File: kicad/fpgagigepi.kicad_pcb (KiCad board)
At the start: 2 copper layers, 1 part, among them U1 24LC32

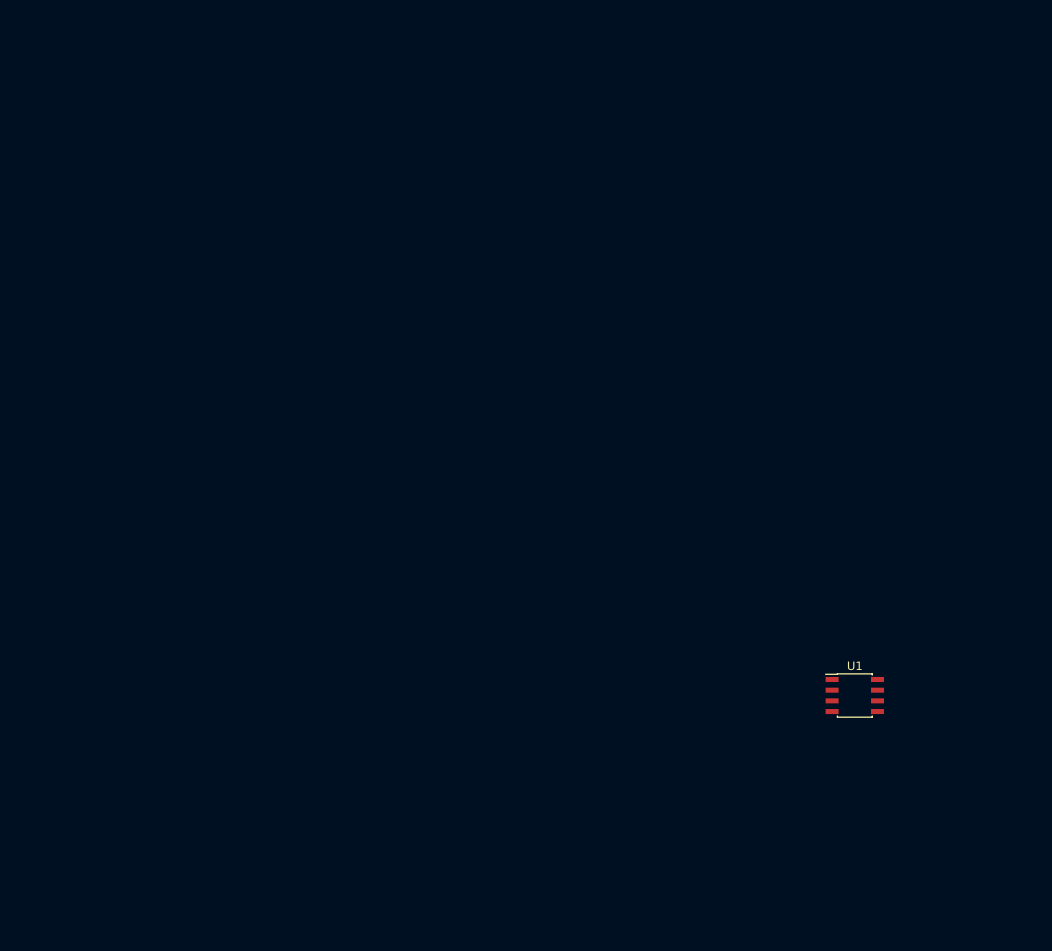
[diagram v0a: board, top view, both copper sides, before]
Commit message: place components to pcb, add footprints of cfps-73 l829 sot-563
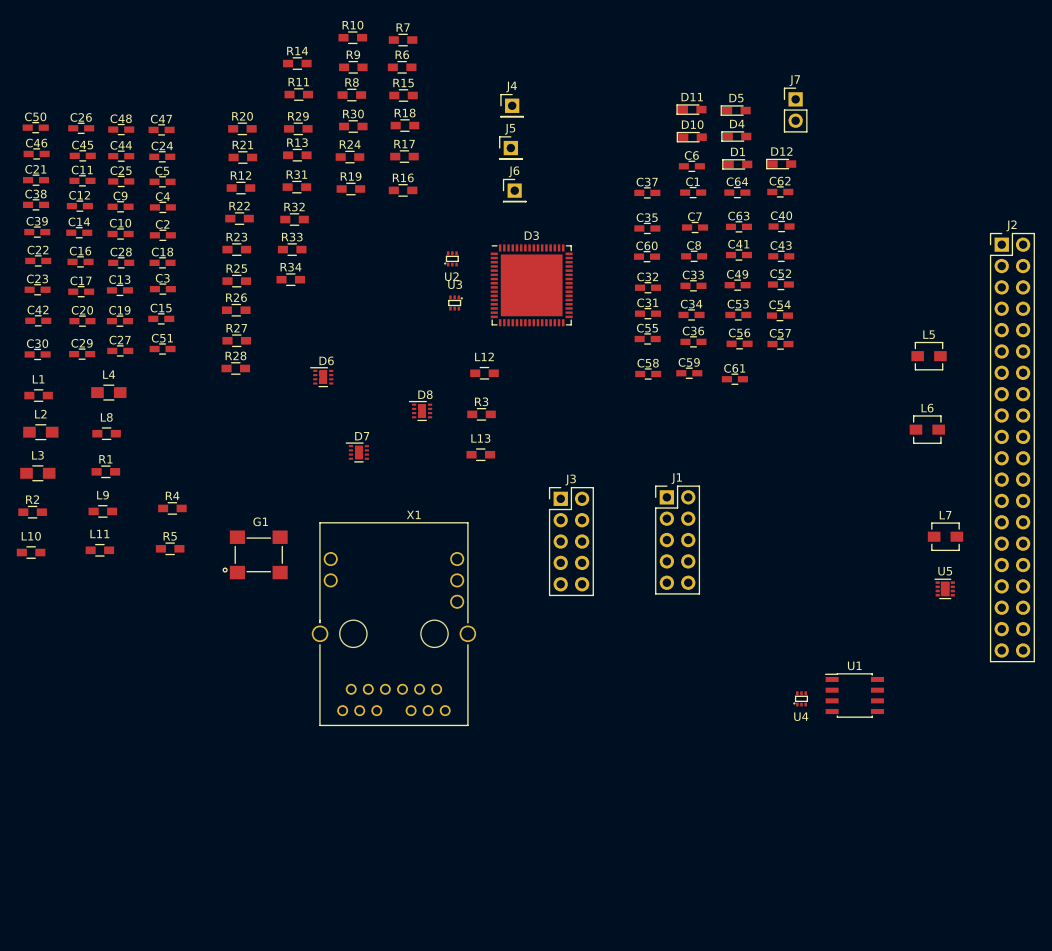
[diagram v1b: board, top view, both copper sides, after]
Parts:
- added C1: 0.1u 16V, Capacitors_SMD:C_0603_HandSoldering, F.Cu at (129.3, 45.2)
- added C10: 22u 6v3, Capacitors_SMD:C_0603_HandSoldering, F.Cu at (61.2, 50.1)
- added C11: 22u 6v3, Capacitors_SMD:C_0603_HandSoldering, F.Cu at (56.6, 43.8)
- added C12: 22u 6v3, Capacitors_SMD:C_0603_HandSoldering, F.Cu at (56.3, 46.8)
- added C13: 10u, Capacitors_SMD:C_0603_HandSoldering, F.Cu at (61.1, 56.8)
- added C14: 10u, Capacitors_SMD:C_0603_HandSoldering, F.Cu at (56.3, 50.0)
- added C15: 0.1u, Capacitors_SMD:C_0603_HandSoldering, F.Cu at (66.0, 60.2)
- added C16: 0.1u, Capacitors_SMD:C_0603_HandSoldering, F.Cu at (56.4, 53.4)
- added C17: 10u, Capacitors_SMD:C_0603_HandSoldering, F.Cu at (56.5, 57.0)
- added C18: 0.1u, Capacitors_SMD:C_0603_HandSoldering, F.Cu at (66.2, 53.5)
- added C19: 0.1u, Capacitors_SMD:C_0603_HandSoldering, F.Cu at (61.1, 60.5)
- added C2: 0.1u 16V, Capacitors_SMD:C_0603_HandSoldering, F.Cu at (66.2, 50.3)
- added C20: 10u, Capacitors_SMD:C_0603_HandSoldering, F.Cu at (56.6, 60.5)
- added C21: 0.1u, Capacitors_SMD:C_0603_HandSoldering, F.Cu at (51.1, 43.7)
- added C22: 0.1u, Capacitors_SMD:C_0603_HandSoldering, F.Cu at (51.4, 53.3)
- added C23: 0.1u, Capacitors_SMD:C_0603_HandSoldering, F.Cu at (51.3, 56.7)
- added C24: 0.1u, Capacitors_SMD:C_0603_HandSoldering, F.Cu at (66.1, 40.9)
- added C25: 0.1u, Capacitors_SMD:C_0603_HandSoldering, F.Cu at (61.3, 43.9)
- added C26: 0.1u, Capacitors_SMD:C_0603_HandSoldering, F.Cu at (56.5, 37.5)
- added C27: 0.1u, Capacitors_SMD:C_0603_HandSoldering, F.Cu at (61.1, 64.0)
- added C28: 0.1u, Capacitors_SMD:C_0603_HandSoldering, F.Cu at (61.3, 53.5)
- added C29: 0.01u, Capacitors_SMD:C_0603_HandSoldering, F.Cu at (56.6, 64.4)
- added C3: 0.1u 16V, Capacitors_SMD:C_0603_HandSoldering, F.Cu at (66.2, 56.7)
- added C30: 0.01u, Capacitors_SMD:C_0603_HandSoldering, F.Cu at (51.3, 64.4)
- added C31: 0.01u, Capacitors_SMD:C_0603_HandSoldering, F.Cu at (123.9, 59.6)
- added C32: 0.01u, Capacitors_SMD:C_0603_HandSoldering, F.Cu at (123.9, 56.5)
- added C33: 0.01u, Capacitors_SMD:C_0603_HandSoldering, F.Cu at (129.3, 56.3)
- added C34: 0.1u, Capacitors_SMD:C_0603_HandSoldering, F.Cu at (129.1, 59.7)
- added C35: 0.01u, Capacitors_SMD:C_0603_HandSoldering, F.Cu at (123.8, 49.5)
- added C36: 0.1u, Capacitors_SMD:C_0603_HandSoldering, F.Cu at (129.3, 62.9)
- added C37: 0.01u, Capacitors_SMD:C_0603_HandSoldering, F.Cu at (123.8, 45.2)
- added C38: 0.1u, Capacitors_SMD:C_0603_HandSoldering, F.Cu at (51.1, 46.6)
- added C39: 0.01u, Capacitors_SMD:C_0603_HandSoldering, F.Cu at (51.3, 49.9)
- added C4: 0.1u 16V, Capacitors_SMD:C_0603_HandSoldering, F.Cu at (66.2, 47.0)
- added C40: 0.1u, Capacitors_SMD:C_0603_HandSoldering, F.Cu at (139.8, 49.2)
- added C41: 0.1u, Capacitors_SMD:C_0603_HandSoldering, F.Cu at (134.7, 52.6)
- added C42: 10u, Capacitors_SMD:C_0603_HandSoldering, F.Cu at (51.4, 60.4)
- added C43: 0.1u, Capacitors_SMD:C_0603_HandSoldering, F.Cu at (139.8, 52.8)
- added C44: 10u, Capacitors_SMD:C_0603_HandSoldering, F.Cu at (61.3, 40.9)
- added C45: 0.1u, Capacitors_SMD:C_0603_HandSoldering, F.Cu at (56.7, 40.8)
- added C46: 0.1u, Capacitors_SMD:C_0603_HandSoldering, F.Cu at (51.2, 40.6)
- added C47: 0.1u, Capacitors_SMD:C_0603_HandSoldering, F.Cu at (66.1, 37.7)
- added C48: 10u, Capacitors_SMD:C_0603_HandSoldering, F.Cu at (61.3, 37.7)
- added C49: 0.1u, Capacitors_SMD:C_0603_HandSoldering, F.Cu at (134.6, 56.2)
- added C5: 0.1u, Capacitors_SMD:C_0603_HandSoldering, F.Cu at (66.2, 43.9)
- added C50: 0.1u, Capacitors_SMD:C_0603_HandSoldering, F.Cu at (51.1, 37.5)
- added C51: 0.1u, Capacitors_SMD:C_0603_HandSoldering, F.Cu at (66.2, 63.8)
- added C52: 0.1u, Capacitors_SMD:C_0603_HandSoldering, F.Cu at (139.7, 56.1)
- added C53: 0.1u, Capacitors_SMD:C_0603_HandSoldering, F.Cu at (134.6, 59.7)
- added C54: 0.1u, Capacitors_SMD:C_0603_HandSoldering, F.Cu at (139.6, 59.8)
- added C55: 0.1u, Capacitors_SMD:C_0603_HandSoldering, F.Cu at (123.9, 62.6)
- added C56: 0.1u, Capacitors_SMD:C_0603_HandSoldering, F.Cu at (134.8, 63.2)
- added C57: 0.1u, Capacitors_SMD:C_0603_HandSoldering, F.Cu at (139.7, 63.2)
- added C58: 0.1u, Capacitors_SMD:C_0603_HandSoldering, F.Cu at (123.9, 66.8)
- added C59: 0.1u, Capacitors_SMD:C_0603_HandSoldering, F.Cu at (128.8, 66.7)
- added C6: 0.1u, Capacitors_SMD:C_0603_HandSoldering, F.Cu at (129.1, 42.1)
- added C60: 10u, Capacitors_SMD:C_0603_HandSoldering, F.Cu at (123.8, 52.8)
- added C61: 10u, Capacitors_SMD:C_0603_HandSoldering, F.Cu at (134.2, 67.4)
- added C62: 10u, Capacitors_SMD:C_0603_HandSoldering, F.Cu at (139.6, 45.1)
- added C63: 0.1u, Capacitors_SMD:C_0603_HandSoldering, F.Cu at (134.7, 49.3)
- added C64: 10u, Capacitors_SMD:C_0603_HandSoldering, F.Cu at (134.5, 45.2)
- added C7: 10u 16V, Capacitors_SMD:C_0603_HandSoldering, F.Cu at (129.5, 49.3)
- added C8: 10u 16V, Capacitors_SMD:C_0603_HandSoldering, F.Cu at (129.4, 52.8)
- added C9: 10u 16V, Capacitors_SMD:C_0603_HandSoldering, F.Cu at (61.2, 46.9)
- added D1: LED, LEDs:LED_0603_HandSoldering, F.Cu at (134.6, 41.8)
- added D10: LED, LEDs:LED_0603_HandSoldering, F.Cu at (129.2, 38.6)
- added D11: LED, LEDs:LED_0603_HandSoldering, F.Cu at (129.2, 35.3)
- added D12: LED, LEDs:LED_0603_HandSoldering, F.Cu at (139.8, 41.8)
- added D3: KSZ9021GN, Housings_DFN_QFN:QFN-64-1EP_9x9mm_Pitch0.5mm, F.Cu at (110.1, 56.2)
- added D4: LED, LEDs:LED_0603_HandSoldering, F.Cu at (134.5, 38.5)
- added D5: LED, LEDs:LED_0603_HandSoldering, F.Cu at (134.4, 35.4)
- added D6: TLV62084, Housings_SON:WSON-8_1EP_2x2mm_Pitch0.5mm, F.Cu at (85.3, 67.1)
- added D7: TLV62084, Housings_SON:WSON-8_1EP_2x2mm_Pitch0.5mm, F.Cu at (89.5, 76.1)
- added D8: TLV62080, Housings_SON:WSON-8_1EP_2x2mm_Pitch0.5mm, F.Cu at (97.0, 71.2)
- added G1: CFPS-73, library:CFPS-73, F.Cu at (77.6, 88.3)
- added J1: Conn_02x05_Odd_Even, Pin_Headers:Pin_Header_Straight_2x05_Pitch2.54mm, F.Cu at (126.1, 81.4)
- added J2: Conn_02x20_Odd_Even, Pin_Headers:Pin_Header_Straight_2x20_Pitch2.54mm, F.Cu at (166.0, 51.4)
- added J3: Conn_02x05_Odd_Even, Pin_Headers:Pin_Header_Straight_2x05_Pitch2.54mm, F.Cu at (113.5, 81.6)
- added J4: Conn_01x01, Pin_Headers:Pin_Header_Straight_1x01_Pitch2.54mm, F.Cu at (107.7, 34.9)
- added J5: Conn_01x01, Pin_Headers:Pin_Header_Straight_1x01_Pitch2.54mm, F.Cu at (107.6, 39.9)
- added J6: Conn_01x01, Pin_Headers:Pin_Header_Straight_1x01_Pitch2.54mm, F.Cu at (108.1, 45.0)
- added J7: Conn_01x02, Pin_Headers:Pin_Header_Straight_1x02_Pitch2.54mm, F.Cu at (141.5, 34.1)
- added L1: BLM18PG330, Inductors_SMD:L_0603_HandSoldering, F.Cu at (51.4, 69.3)
- added L10: BLM18PG330, Inductors_SMD:L_0603_HandSoldering, F.Cu at (50.5, 88.0)
- added L11: BLM18PG330, Inductors_SMD:L_0603_HandSoldering, F.Cu at (58.7, 87.7)
- added L12: BLM18PG330, Inductors_SMD:L_0603_HandSoldering, F.Cu at (104.5, 66.7)
- added L13: BLM18PG330, Inductors_SMD:L_0603_HandSoldering, F.Cu at (104.0, 76.4)
- added L2: BLM21PG300, Inductors_SMD:L_0805_HandSoldering, F.Cu at (51.7, 73.7)
- added L3: BLM21PG300, Inductors_SMD:L_0805_HandSoldering, F.Cu at (51.3, 78.6)
- added L4: BLM21PG300, Inductors_SMD:L_0805_HandSoldering, F.Cu at (59.8, 69.0)
- added L5: LQH3NPN1R0NJ0L, Inductors_SMD:L_Vishay_IHLP-1212, F.Cu at (157.3, 64.6)
- added L6: LQH3NPN1R0NJ0L, Inductors_SMD:L_Vishay_IHLP-1212, F.Cu at (157.1, 73.4)
- added L7: LQH3NPN1R0NJ0L, Inductors_SMD:L_Vishay_IHLP-1212, F.Cu at (159.3, 86.1)
- added L8: BLM18PG330, Inductors_SMD:L_0603_HandSoldering, F.Cu at (59.5, 73.9)
- added L9: BLM18PG330, Inductors_SMD:L_0603_HandSoldering, F.Cu at (59.1, 83.1)
- added R1: 3.9k, Resistors_SMD:R_0603_HandSoldering, F.Cu at (59.4, 78.4)
- added R10: 39.2k 1%, Resistors_SMD:R_0603_HandSoldering, F.Cu at (88.8, 26.8)
- added R11: 178k 1%, Resistors_SMD:R_0603_HandSoldering, F.Cu at (82.4, 33.5)
- added R12: 39.2k 1%, Resistors_SMD:R_0603_HandSoldering, F.Cu at (75.5, 44.6)
- added R13: 10k, Resistors_SMD:R_0603_HandSoldering, F.Cu at (82.2, 40.7)
- added R14: 4.7k, Resistors_SMD:R_0603_HandSoldering, F.Cu at (82.2, 29.8)
- added R15: 390, Resistors_SMD:R_0603_HandSoldering, F.Cu at (94.8, 33.6)
- added R16: 390, Resistors_SMD:R_0603_HandSoldering, F.Cu at (94.8, 44.9)
- added R17: 390, Resistors_SMD:R_0603_HandSoldering, F.Cu at (94.9, 40.9)
- added R18: 390, Resistors_SMD:R_0603_HandSoldering, F.Cu at (95.0, 37.2)
- added R19: 10k, Resistors_SMD:R_0603_HandSoldering, F.Cu at (88.6, 44.8)
- added R2: 3.9k, Resistors_SMD:R_0603_HandSoldering, F.Cu at (50.7, 83.2)
- added R20: 10k, Resistors_SMD:R_0603_HandSoldering, F.Cu at (75.7, 37.6)
- added R21: 4.7k, Resistors_SMD:R_0603_HandSoldering, F.Cu at (75.7, 41.0)
- added R22: 220, Resistors_SMD:R_0603_HandSoldering, F.Cu at (75.3, 48.3)
- added R23: 220, Resistors_SMD:R_0603_HandSoldering, F.Cu at (75.0, 52.0)
- added R24: 10k, Resistors_SMD:R_0603_HandSoldering, F.Cu at (88.5, 41.0)
- added R25: 1k, Resistors_SMD:R_0603_HandSoldering, F.Cu at (75.0, 55.7)
- added R26: 1k, Resistors_SMD:R_0603_HandSoldering, F.Cu at (74.9, 59.2)
- added R27: 1k, Resistors_SMD:R_0603_HandSoldering, F.Cu at (75.0, 62.8)
- added R28: 10k, Resistors_SMD:R_0603_HandSoldering, F.Cu at (74.9, 66.1)
- added R29: 10k, Resistors_SMD:R_0603_HandSoldering, F.Cu at (82.3, 37.6)
- added R3: 1k, Resistors_SMD:R_0603_HandSoldering, F.Cu at (104.1, 71.6)
- added R30: 10k, Resistors_SMD:R_0603_HandSoldering, F.Cu at (88.8, 37.3)
- added R31: 10k, Resistors_SMD:R_0603_HandSoldering, F.Cu at (82.1, 44.5)
- added R32: 390, Resistors_SMD:R_0603_HandSoldering, F.Cu at (81.9, 48.4)
- added R33: 390, Resistors_SMD:R_0603_HandSoldering, F.Cu at (81.6, 52.0)
- added R34: 4.99k 1%, Resistors_SMD:R_0603_HandSoldering, F.Cu at (81.4, 55.5)
- added R4: 10k, Resistors_SMD:R_0603_HandSoldering, F.Cu at (67.3, 82.8)
- added R5: 10k, Resistors_SMD:R_0603_HandSoldering, F.Cu at (67.1, 87.6)
- added R6: 1k, Resistors_SMD:R_0603_HandSoldering, F.Cu at (94.7, 30.3)
- added R7: 178k 1%, Resistors_SMD:R_0603_HandSoldering, F.Cu at (94.8, 27.0)
- added R8: 28k 1%, Resistors_SMD:R_0603_HandSoldering, F.Cu at (88.7, 33.6)
- added R9: 65.3k 1%, Resistors_SMD:R_0603_HandSoldering, F.Cu at (88.8, 30.3)
- added U2: NUP4114UPXV6T1G, library:SOT-563-6, F.Cu at (100.6, 53.1)
- added U3: NUP4114UPXV6T1G, library:SOT-563-6, F.Cu at (100.9, 58.3)
- added U4: NUP4114UPXV6T1G, library:SOT-563-6, F.Cu at (142.2, 105.4)
- added U5: NB3L553, Housings_DFN_QFN:DFN-8-1EP_2x2mm_Pitch0.5mm, F.Cu at (159.3, 92.3)
- added X1: L829-1J1T-43, library:L829, F.Cu at (93.7, 97.7)

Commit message: add modeles to 3d render
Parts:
- added D2: 10cl025, library:EQFP-144_20x20mm_Pitch0.5mm, F.Cu at (120.3, 92.3)
- C11, C12, C14, C21, C24, C25, C26, C38, C39, C44, C45, C46, C47, C48, C5, C50, C52, C54, C62, C9, L11, L12, L8, L9, R1, R3: moved to B.Cu
- D6, D7, D8: footprint Housings_SON:WSON-8_1EP_2x2mm_Pitch0.5mm -> library:WSON-8_1EP_2x2mm_Pitch0.5mm
- J2: footprint Pin_Headers:Pin_Header_Straight_2x20_Pitch2.54mm -> Socket_Strips:Socket_Strip_Straight_2x20_Pitch2.54mm; moved to B.Cu
- L5, L6, L7: footprint Inductors_SMD:L_Vishay_IHLP-1212 -> library:L_Vishay_IHLP-1212
- moved R2 106.0 mm to (156.3, 92.2)
- moved R7 105.9 mm to (143.8, 120.9)
- moved R6 104.6 mm to (143.8, 122.6)
- moved R14 104.1 mm to (131.2, 121.7)
- moved R9 103.8 mm to (139.5, 120.9)
- moved R8 102.5 mm to (139.5, 122.6)
- moved R33 102.3 mm to (156.0, 122.1)
- moved R10 101.1 mm to (123.3, 121.8), turned to 180 degrees
- moved C29 97.6 mm to (135.9, 121.3), turned to 90 degrees
- moved C50 97.4 mm to (108.7, 116.0)
- moved C26 97.2 mm to (114.1, 115.9)
- moved C48 97.0 mm to (118.9, 115.7)
- moved C47 96.9 mm to (123.7, 115.7)
- moved L2 93.9 mm to (143.4, 93.8)
- moved C46 92.4 mm to (108.8, 112.8)
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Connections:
- J4 pad 1: +3V3 -> Net-(C10-Pad1)
- J5 pad 1: +1V2 -> Net-(C11-Pad1)
- J6 pad 1: +2V5 -> Net-(C12-Pad1)
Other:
- board outline added: 65 x 56.5 mm

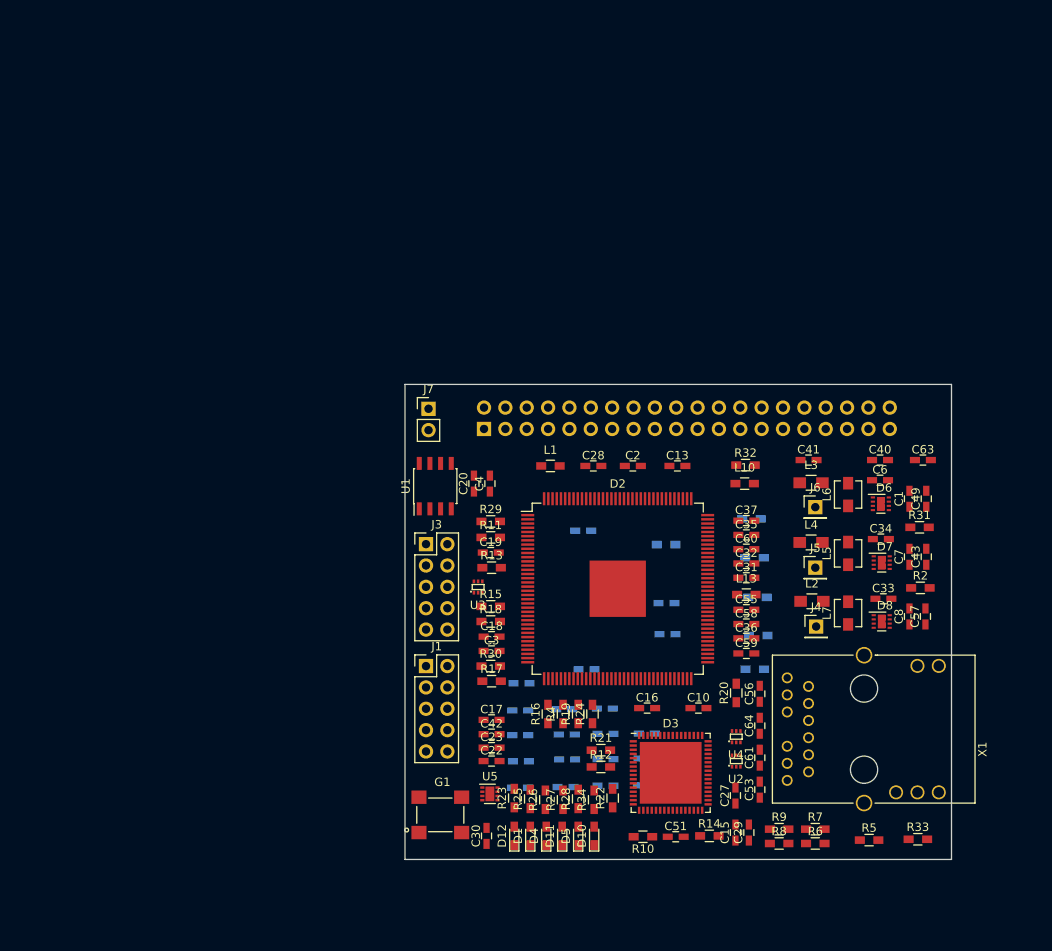
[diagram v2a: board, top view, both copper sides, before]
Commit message: Project translated to template "Raspberry Pi HAT" Added library files from template. Renamed refdes. Changed placement for all components
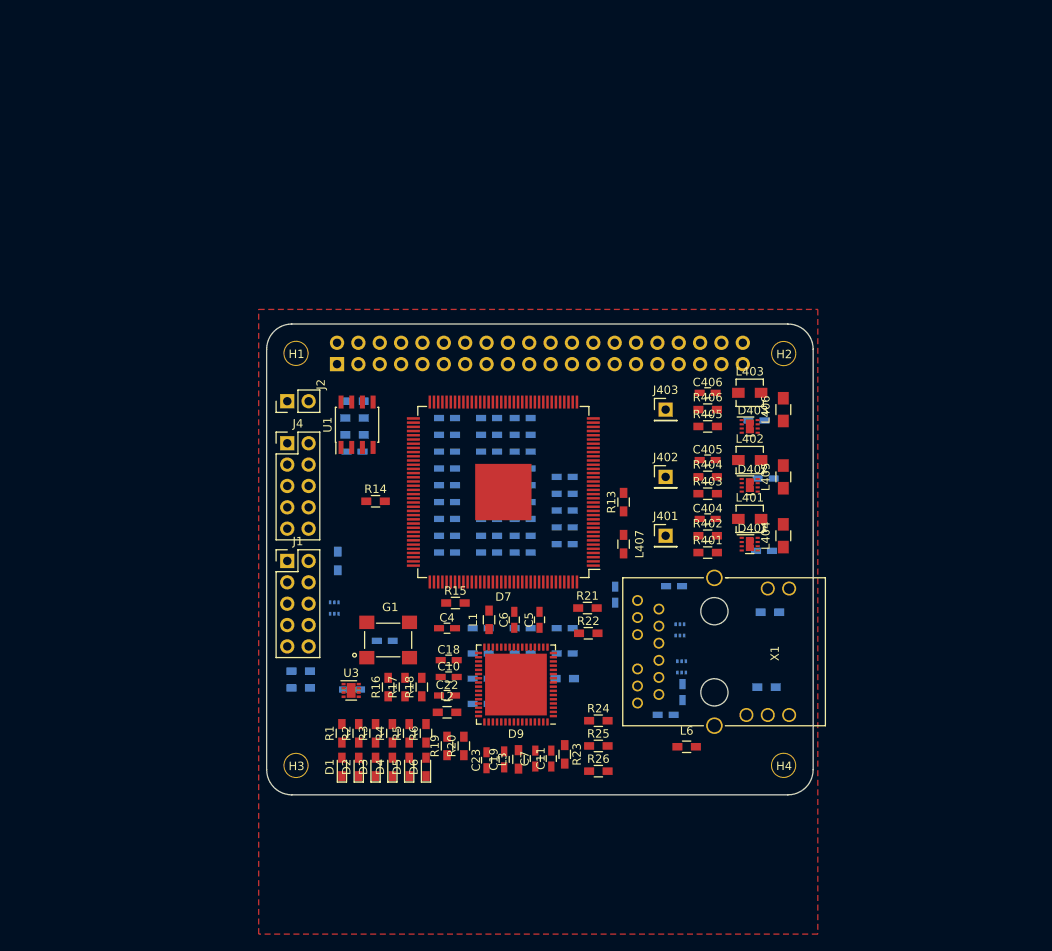
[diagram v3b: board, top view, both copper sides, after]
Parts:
- removed C27, C28, C34, C36, C38, C40, C41, C43, C45, C46, C47, C49, C50, C51, C52, C53, C54, C55, C56, C57, C58, C59, C63: 0.1u, Capacitors_SMD:C_0603_HandSoldering
- removed C29, C30, C31, C32, C33, C35, C37, C39: 0.01u, Capacitors_SMD:C_0603_HandSoldering
- removed C42, C44, C48, C60, C61, C62, C64: 10u, Capacitors_SMD:C_0603_HandSoldering
- removed D10, D11, D12: LED, LEDs:LED_0603_HandSoldering
- removed D8: TLV62080, library:WSON-8_1EP_2x2mm_Pitch0.5mm
- removed J5, J6: Conn_01x01, Pin_Headers:Pin_Header_Straight_1x01_Pitch2.54mm
- removed J7: Conn_01x02, Pin_Headers:Pin_Header_Straight_1x02_Pitch2.54mm
- removed L10, L11, L12, L13, L8, L9: BLM18PG330, Inductors_SMD:L_0603_HandSoldering
- removed L7: LQH3NPN1R0NJ0L, library:L_Vishay_IHLP-1212
- removed R29, R30, R31: 10k, Resistors_SMD:R_0603_HandSoldering
- removed R32, R33: 390, Resistors_SMD:R_0603_HandSoldering
- removed R34: 4.99k 1%, Resistors_SMD:R_0603_HandSoldering
- added C401: 10u 16V, Capacitors_SMD:C_0603_HandSoldering, B.Cu at (137.7, 87.8)
- added C402: 10u 16V, Capacitors_SMD:C_0603_HandSoldering, B.Cu at (137.9, 79.2)
- added C403: 10u 16V, Capacitors_SMD:C_0603_HandSoldering, B.Cu at (136.8, 72.3)
- added C404: 22u 6v3, Capacitors_SMD:C_0603_HandSoldering, F.Cu at (131.0, 84.0)
- added C405: 22u 6v3, Capacitors_SMD:C_0603_HandSoldering, F.Cu at (131.0, 77.0)
- added C406: 22u 6v3, Capacitors_SMD:C_0603_HandSoldering, F.Cu at (131.0, 69.0)
- added C407: 10u, Capacitors_SMD:C_0603_HandSoldering, B.Cu at (109.0, 86.0)
- added C408: 10u, Capacitors_SMD:C_0603_HandSoldering, B.Cu at (105.0, 88.0)
- added C409: 0.1u, Capacitors_SMD:C_0603_HandSoldering, B.Cu at (105.0, 84.0)
- added C410: 0.1u, Capacitors_SMD:C_0603_HandSoldering, B.Cu at (100.0, 86.0)
- added C411: 10u, Capacitors_SMD:C_0603_HandSoldering, B.Cu at (105.0, 80.0)
- added C412: 0.1u, Capacitors_SMD:C_0603_HandSoldering, B.Cu at (109.0, 80.0)
- added C413: 0.1u, Capacitors_SMD:C_0603_HandSoldering, B.Cu at (109.0, 78.0)
- added C414: 10u, Capacitors_SMD:C_0603_HandSoldering, B.Cu at (109.0, 84.0)
- added C415: 0.1u, Capacitors_SMD:C_0603_HandSoldering, B.Cu at (100.0, 88.0)
- added C416: 0.1u, Capacitors_SMD:C_0603_HandSoldering, B.Cu at (100.0, 84.0)
- added C417: 0.1u, Capacitors_SMD:C_0603_HandSoldering, B.Cu at (100.0, 82.0)
- added C418: 0.1u, Capacitors_SMD:C_0603_HandSoldering, B.Cu at (105.0, 76.0)
- added C419: 0.1u, Capacitors_SMD:C_0603_HandSoldering, B.Cu at (100.0, 80.0)
- added C420: 0.1u, Capacitors_SMD:C_0603_HandSoldering, B.Cu at (105.0, 86.0)
- added C421: 0.1u, Capacitors_SMD:C_0603_HandSoldering, B.Cu at (105.0, 78.0)
- added C422: 0.1u, Capacitors_SMD:C_0603_HandSoldering, B.Cu at (109.0, 82.0)
- added C423: 0.01u, Capacitors_SMD:C_0603_HandSoldering, B.Cu at (105.0, 74.0)
- added C424: 0.01u, Capacitors_SMD:C_0603_HandSoldering, B.Cu at (100.0, 78.0)
- added C425: 0.01u, Capacitors_SMD:C_0603_HandSoldering, B.Cu at (105.0, 82.0)
- added C426: 0.01u, Capacitors_SMD:C_0603_HandSoldering, B.Cu at (100.0, 74.0)
- added C427: 0.01u, Capacitors_SMD:C_0603_HandSoldering, B.Cu at (114.0, 83.0)
- added C428: 0.1u, Capacitors_SMD:C_0603_HandSoldering, B.Cu at (114.0, 85.0)
- added C429: 0.01u, Capacitors_SMD:C_0603_HandSoldering, B.Cu at (100.0, 76.0)
- added C430: 0.1u, Capacitors_SMD:C_0603_HandSoldering, B.Cu at (114.0, 81.0)
- added C431: 0.01u, Capacitors_SMD:C_0603_HandSoldering, B.Cu at (114.0, 87.0)
- added C432: 0.1u, Capacitors_SMD:C_0603_HandSoldering, B.Cu at (114.0, 79.0)
- added C433: 0.01u, Capacitors_SMD:C_0603_HandSoldering, B.Cu at (109.0, 72.0)
- added C434: 0.1u, Capacitors_SMD:C_0603_HandSoldering, B.Cu at (109.0, 88.0)
- added C435: 0.1u, Capacitors_SMD:C_0603_HandSoldering, B.Cu at (105.0, 72.0)
- added C436: 10u, Capacitors_SMD:C_0603_HandSoldering, B.Cu at (109.0, 76.0)
- added C437: 0.1u, Capacitors_SMD:C_0603_HandSoldering, B.Cu at (100.0, 72.0)
- added C438: 10u, Capacitors_SMD:C_0603_HandSoldering, B.Cu at (109.0, 74.0)
- added D401: TLV62084, library:WSON-8_1EP_2x2mm_Pitch0.5mm, F.Cu at (136.0, 87.0)
- added D402: TLV62084, library:WSON-8_1EP_2x2mm_Pitch0.5mm, F.Cu at (136.0, 80.0)
- added D403: TLV62080, library:WSON-8_1EP_2x2mm_Pitch0.5mm, F.Cu at (136.0, 73.0)
- added D9: KSZ9021GN, Housings_DFN_QFN:QFN-64-1EP_9x9mm_Pitch0.5mm, F.Cu at (108.2, 103.7)
- added H1: 3mm_Mounting_Hole, project_footprints:NPTH_3mm_ID, F.Cu at (82.0, 64.3)
- added H2: 3mm_Mounting_Hole, project_footprints:NPTH_3mm_ID, F.Cu at (140.0, 64.3)
- added H3: 3mm_Mounting_Hole, project_footprints:NPTH_3mm_ID, F.Cu at (82.0, 113.3)
- added H4: 3mm_Mounting_Hole, project_footprints:NPTH_3mm_ID, F.Cu at (140.0, 113.3)
- added J401: Conn_01x01, Pin_Headers:Pin_Header_Straight_1x01_Pitch2.54mm, F.Cu at (126.0, 86.0)
- added J402: Conn_01x01, Pin_Headers:Pin_Header_Straight_1x01_Pitch2.54mm, F.Cu at (126.0, 79.0)
- added J403: Conn_01x01, Pin_Headers:Pin_Header_Straight_1x01_Pitch2.54mm, F.Cu at (126.0, 71.0)
- added L401: LQH3NPN1R0NJ0L, library:L_Vishay_IHLP-1212, F.Cu at (136.0, 84.0)
- added L402: LQH3NPN1R0NJ0L, library:L_Vishay_IHLP-1212, F.Cu at (136.0, 77.0)
- added L403: LQH3NPN1R0NJ0L, library:L_Vishay_IHLP-1212, F.Cu at (136.0, 69.0)
- added L404: BLM21PG300, Inductors_SMD:L_0805_HandSoldering, F.Cu at (140.0, 86.0)
- added L405: BLM21PG300, Inductors_SMD:L_0805_HandSoldering, F.Cu at (140.0, 79.0)
- added L406: BLM21PG300, Inductors_SMD:L_0805_HandSoldering, F.Cu at (140.0, 71.0)
- added L407: BLM18PG330, Inductors_SMD:L_0603_HandSoldering, F.Cu at (121.0, 87.0)
- added R401: 178k 1%, Resistors_SMD:R_0603_HandSoldering, F.Cu at (131.0, 88.0)
- added R402: 28k 1%, Resistors_SMD:R_0603_HandSoldering, F.Cu at (131.0, 86.0)
- added R403: 65.3k 1%, Resistors_SMD:R_0603_HandSoldering, F.Cu at (131.0, 81.0)
- added R404: 39.2k 1%, Resistors_SMD:R_0603_HandSoldering, F.Cu at (131.0, 79.0)
- added R405: 178k 1%, Resistors_SMD:R_0603_HandSoldering, F.Cu at (131.0, 73.0)
- added R406: 39.2k 1%, Resistors_SMD:R_0603_HandSoldering, F.Cu at (131.0, 71.0)
- C1, C2, C3: value 0.1u 16V -> 0.1u; moved to B.Cu
- C10, C12: value 22u 6v3 -> 0.1u
- C11: value 22u 6v3 -> 0.1u; moved to F.Cu
- C13, C20: value 10u -> 0.1u; moved to B.Cu
- C14: value 10u -> 0.1u 16V
- C15, C16: value 0.1u -> 0.1u 16V; moved to B.Cu
- C17: value 10u -> 0.1u 16V; moved to B.Cu
- C22, C23, C24, C26, C6: value 0.1u -> 10u
- C4: value 0.1u 16V -> 0.1u
- C5: moved to F.Cu
- C7, C9: value 10u 16V -> 0.1u
- C8: value 10u 16V -> 0.1u; moved to B.Cu
- D2: value 10cl025 -> LED; footprint library:EQFP-144_20x20mm_Pitch0.5mm -> LEDs:LED_0603_HandSoldering
- D3: value KSZ9021GN -> LED; footprint Housings_DFN_QFN:QFN-64-1EP_9x9mm_Pitch0.5mm -> LEDs:LED_0603_HandSoldering
- D6: value TLV62084 -> LED; footprint library:WSON-8_1EP_2x2mm_Pitch0.5mm -> LEDs:LED_0603_HandSoldering
- D7: value TLV62084 -> 10cl025; footprint library:WSON-8_1EP_2x2mm_Pitch0.5mm -> library:EQFP-144_20x20mm_Pitch0.5mm
- J2: value Conn_02x20_Odd_Even -> Conn_01x02; footprint Socket_Strips:Socket_Strip_Straight_2x20_Pitch2.54mm -> Pin_Headers:Pin_Header_Straight_1x02_Pitch2.54mm; moved to F.Cu
- J3: value Conn_02x05_Odd_Even -> OX40HAT; footprint Pin_Headers:Pin_Header_Straight_2x05_Pitch2.54mm -> Socket_Strips:Socket_Strip_Straight_2x20_Pitch2.54mm; moved to B.Cu
- J4: value Conn_01x01 -> Conn_02x05_Odd_Even; footprint Pin_Headers:Pin_Header_Straight_1x01_Pitch2.54mm -> Pin_Headers:Pin_Header_Straight_2x05_Pitch2.54mm
- L2, L3: value BLM21PG300 -> BLM18PG330; footprint Inductors_SMD:L_0805_HandSoldering -> Inductors_SMD:L_0603_HandSoldering
- L4: value BLM21PG300 -> BLM18PG330; footprint Inductors_SMD:L_0805_HandSoldering -> Inductors_SMD:L_0603_HandSoldering; moved to B.Cu
- L5: value LQH3NPN1R0NJ0L -> BLM18PG330; footprint library:L_Vishay_IHLP-1212 -> Inductors_SMD:L_0603_HandSoldering; moved to B.Cu
- L6: value LQH3NPN1R0NJ0L -> BLM18PG330; footprint library:L_Vishay_IHLP-1212 -> Inductors_SMD:L_0603_HandSoldering
- R1: value 3.9k -> 390; moved to F.Cu
- R10: value 39.2k 1% -> 3.9k; moved to B.Cu
- R11: value 178k 1% -> 3.9k; moved to B.Cu
- R12: value 39.2k 1% -> 1k; moved to B.Cu
- R14: value 4.7k -> 10k
- R15, R16: value 390 -> 10k
- R17, R18: value 390 -> 1k
- R19: value 10k -> 1k
- R2: value 3.9k -> 390
- R20: value 10k -> 4.7k
- R22: value 220 -> 10k
- R23: value 220 -> 4.99k 1%
- R25, R26: value 1k -> 10k
- R27: value 1k -> 220; moved to B.Cu
- R28: value 10k -> 220; moved to B.Cu
- R3: value 1k -> 390; moved to F.Cu
- R4, R5: value 10k -> 390
- R6: value 1k -> 390
- R7: value 178k 1% -> 10k; moved to B.Cu
- R8: value 28k 1% -> 10k; moved to B.Cu
- R9: value 65.3k 1% -> 1k; moved to B.Cu
- U2, U4: moved to B.Cu
- U3: value NUP4114UPXV6T1G -> NB3L553; footprint library:SOT-563-6 -> Housings_DFN_QFN:DFN-8-1EP_2x2mm_Pitch0.5mm
- U5: value NB3L553 -> NUP4114UPXV6T1G; footprint Housings_DFN_QFN:DFN-8-1EP_2x2mm_Pitch0.5mm -> library:SOT-563-6; moved to B.Cu
- moved R2 69.0 mm to (89.5, 109.5), turned to 90 degrees
- moved J4 66.6 mm to (81.0, 75.0)
- moved C1 64.6 mm to (92.6, 98.5), turned to 0 degrees
- moved R7 63.5 mm to (82.6, 104.1)
- moved D6 62.5 mm to (97.5, 113.5), turned to 90 degrees
- moved R9 61.4 mm to (87.0, 89.0), turned to 90 degrees
- moved R8 60.5 mm to (82.6, 102.1)
- moved R10 60.5 mm to (89.0, 72.0), turned to 0 degrees
- moved R14 56.2 mm to (91.5, 81.9)
- moved R5 56.2 mm to (95.5, 109.5), turned to 90 degrees
- moved R1 52.0 mm to (87.5, 109.5), turned to 90 degrees
- moved U2 51.1 mm to (86.6, 94.6)
- moved C8 51.0 mm to (104.0, 97.0), turned to 0 degrees
- moved C7 50.6 mm to (110.5, 112.5)
- moved R12 49.2 mm to (89.0, 74.0)
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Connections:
- C1 pad 1: /ethernet/TACT1 -> +3V3
- C11 pad 1: Net-(C11-Pad1) -> DVDDH
- C12 pad 1: Net-(C12-Pad1) -> AVDDL
- C13 pad 1: +3V3 -> DVDDL
- C14 pad 1: +3V3 -> /ethernet.sch/TACT1
- C15 pad 1: +3V3 -> /ethernet.sch/TACT2
- C16 pad 1: +3V3 -> /ethernet.sch/TACT3
- C17 pad 1: Net-(C17-Pad1) -> /ethernet.sch/TACT4
- C18 pad 1: +3V3 -> Net-(C10-Pad1)
- C19 pad 1: +3V3 -> DVDDH
- C2 pad 1: /ethernet/TACT2 -> +3V3
- C20 pad 1: +2V5 -> AVDDL
- C21 pad 1: Net-(C17-Pad1) -> DVDDL
- C22 pad 1: +3V3 -> Net-(C10-Pad1)
- C23 pad 1: +3V3 -> DVDDH
- C24 pad 1: +2V5 -> AVDDL
- C25 pad 1: Net-(C17-Pad1) -> DVDDL
- C26 pad 1: +3V3 -> DVDDL
- C3 pad 1: /ethernet/TACT3 -> +3V3
- C4 pad 1: /ethernet/TACT4 -> /ethernet.sch/RESET_N
- C5 pad 1: +3V3 -> Net-(C5-Pad1)
- C6 pad 1: +3V3 -> Net-(C5-Pad1)
- C7 pad 1: +5V -> DVDDH
- C8 pad 1: +5V -> AVDDL
- C9 pad 1: +5V -> DVDDL
- D2 pad 1: Net-(C17-Pad1) -> USER_LED0
- D2 pad 2: GND -> Net-(D2-Pad2)
- D3 pad 1: Net-(C52-Pad1) -> USER_LED1
- D3 pad 2: /ethernet/TXRXP_A -> Net-(D3-Pad2)
- D6 pad 1: +5V -> GND
- D6 pad 2: GND -> Net-(D6-Pad2)
- D7 pad 1: +5V -> Net-(C411-Pad1)
- D7 pad 3: GND -> +2V5
- D7 pad 4: Net-(D7-Pad4) -> GND
- D7 pad 5: Net-(C11-Pad1) -> +1V2
- D7 pad 6: Net-(D7-Pad6) -> IO_6
- D7 pad 7: Net-(D7-Pad7) -> INT_N
- D7 pad 8: +5V -> IO_8
- D7 pad 9: GND -> nSTATUS
- G1 pad 1: Net-(G1-Pad1) -> (no net)
- J1 pad 1: +5V -> JTAG_TCK
- J1 pad 10: UART0_RX -> GND
- J1 pad 2: /interface/IO_44 -> GND
- J1 pad 3: /interface/IO_39 -> JTAG_TDO
- J1 pad 4: /interface/IO_46 -> +3V3
- J1 pad 5: /interface/IO_42 -> JTAG_TMS
- J1 pad 6: /interface/IO_49 -> (no net)
- J1 pad 7: /interface/IO_43 -> (no net)
- J1 pad 8: UART0_TX -> (no net)
- J1 pad 9: GND -> JTAG_TDI
- J2 pad 2: +5V -> GND
- J3 pad 1: JTAG_TCK -> (no net)
- J3 pad 10: GND -> UART0_RX
- J3 pad 2: GND -> +5V
- J3 pad 3: JTAG_TDO -> SDA
- J3 pad 4: +3V3 -> +5V
- J3 pad 5: JTAG_TMS -> SCL
- J3 pad 6: Net-(J3-Pad6) -> GND
- J3 pad 7: Net-(J3-Pad7) -> IO_50
- J3 pad 8: Net-(J3-Pad8) -> UART0_TX
- J3 pad 9: JTAG_TDI -> Net-(J3-Pad25)
- J4 pad 1: Net-(C10-Pad1) -> +5V
- L1 pad 1: Net-(L1-Pad1) -> Net-(C5-Pad1)
- L1 pad 2: GND -> +1V2
- L3 pad 1: Net-(C11-Pad1) -> DVDDH
- L3 pad 2: +1V2 -> +3V3
- L4 pad 1: Net-(C12-Pad1) -> AVDDL
- L4 pad 2: +2V5 -> +1V2
- L5 pad 1: Net-(D6-Pad7) -> DVDDL
- L5 pad 2: Net-(C10-Pad1) -> +1V2
- L6 pad 1: Net-(D7-Pad7) -> Net-(L6-Pad1)
- L6 pad 2: Net-(C11-Pad1) -> GND
- R1 pad 1: +3V3 -> Net-(D1-Pad2)
- R1 pad 2: SDA -> +3V3
- R10 pad 1: GND -> +3V3
- R10 pad 2: Net-(D7-Pad4) -> SDA
- R11 pad 1: Net-(C12-Pad1) -> +3V3
- R11 pad 2: Net-(D8-Pad4) -> SCL
- R12 pad 1: GND -> +3V3
- R12 pad 2: Net-(D8-Pad4) -> Net-(J2-Pad1)
- R13 pad 1: +3V3 -> nSTATUS
- R13 pad 2: /ethernet/RESET_N -> +3V3
- R14 pad 1: /ethernet/MDIO -> +3V3
- R14 pad 2: +3V3 -> CONF_DONE
- R15 pad 1: Net-(D10-Pad2) -> +3V3
- R15 pad 2: +3V3 -> /ethernet.sch/RESET_N
- R16 pad 1: Net-(D11-Pad2) -> /ethernet.sch/RXD0
- R16 pad 2: +3V3 -> DVDDH
- R17 pad 1: Net-(D12-Pad2) -> /ethernet.sch/RXD1
- R17 pad 2: +3V3 -> GND
- R18 pad 1: Net-(D1-Pad2) -> /ethernet.sch/RXD2
- R18 pad 2: +3V3 -> GND
- R19 pad 1: nSTATUS -> /ethernet.sch/RXD3
- R19 pad 2: +3V3 -> GND
- R2 pad 1: +3V3 -> Net-(D2-Pad2)
- R2 pad 2: SCL -> +3V3
- R20 pad 1: +3V3 -> /ethernet.sch/MDIO
- R20 pad 2: CONF_DONE -> +3V3
- R22 pad 1: Net-(R22-Pad1) -> CLK_125M
- R23 pad 1: DVDDH -> Net-(D9-Pad63)
- R23 pad 2: Net-(R23-Pad2) -> GND
- R24 pad 1: /ethernet/RXD0 -> DVDDH
- R24 pad 2: DVDDH -> MDI_LED_G
- R25 pad 1: /ethernet/RXD1 -> DVDDH
- R25 pad 2: GND -> MDI_LED_Y
- R26 pad 1: /ethernet/RXD2 -> DVDDH
- R26 pad 2: GND -> /ethernet.sch/RX_CLK
- R27 pad 1: /ethernet/RXD3 -> Net-(R27-Pad1)
- R27 pad 2: GND -> DVDDH
- R28 pad 1: CLK_125M -> DVDDH
- R28 pad 2: DVDDH -> Net-(R28-Pad2)
- R3 pad 1: +3V3 -> Net-(D3-Pad2)
- R3 pad 2: Net-(J7-Pad1) -> +3V3
- R4 pad 1: +3V3 -> Net-(D4-Pad2)
- R4 pad 2: JTAG_TDI -> +3V3
- R5 pad 1: +3V3 -> Net-(D5-Pad2)
- R5 pad 2: JTAG_TMS -> +3V3
- R6 pad 1: GND -> Net-(D6-Pad2)
- R6 pad 2: JTAG_TCK -> +3V3
- R7 pad 1: Net-(C10-Pad1) -> +3V3
- R7 pad 2: Net-(D6-Pad4) -> JTAG_TDI
- R8 pad 1: GND -> +3V3
- R8 pad 2: Net-(D6-Pad4) -> JTAG_TMS
- R9 pad 1: Net-(C11-Pad1) -> GND
- R9 pad 2: Net-(D7-Pad4) -> JTAG_TCK
- U1 pad 7: Net-(J7-Pad1) -> Net-(J2-Pad1)
- U2 pad 1: /ethernet/TXRXP_A -> JTAG_TDO
- U2 pad 2: Net-(U2-Pad2) -> GND
- U2 pad 3: /ethernet/TXRXM_A -> JTAG_TMS
- U2 pad 4: /ethernet/TXRXP_B -> JTAG_TDI
- U2 pad 5: Net-(U2-Pad5) -> +3V3
- U2 pad 6: /ethernet/TXRXM_B -> JTAG_TCK
- U3 pad 1: /ethernet/TXRXP_C -> +3V3
- U3 pad 2: Net-(U3-Pad2) -> 25M_A
- U3 pad 3: /ethernet/TXRXM_C -> 25M_B
- U3 pad 4: /ethernet/TXRXP_D -> GND
- U3 pad 5: Net-(U3-Pad5) -> Net-(G1-Pad3)
- U3 pad 6: /ethernet/TXRXM_D -> (no net)
- U4 pad 1: JTAG_TDO -> /ethernet.sch/TXRXP_A
- U4 pad 2: GND -> (no net)
- U4 pad 3: JTAG_TMS -> /ethernet.sch/TXRXM_A
- U4 pad 4: JTAG_TDI -> /ethernet.sch/TXRXP_B
- U4 pad 5: +3V3 -> (no net)
- U4 pad 6: JTAG_TCK -> /ethernet.sch/TXRXM_B
- U5 pad 1: +3V3 -> /ethernet.sch/TXRXP_C
- U5 pad 2: 25M_A -> (no net)
- U5 pad 3: 25M_B -> /ethernet.sch/TXRXM_C
- U5 pad 4: GND -> /ethernet.sch/TXRXP_D
- U5 pad 5: Net-(G1-Pad3) -> (no net)
- U5 pad 6: Net-(U5-Pad6) -> /ethernet.sch/TXRXM_D
- X1 pad 1: /ethernet/TACT3 -> /ethernet.sch/TACT3
- X1 pad 10: /ethernet/TXRXM_A -> /ethernet.sch/TXRXM_A
- X1 pad 11: /ethernet/TXRXP_A -> /ethernet.sch/TXRXP_A
- X1 pad 12: /ethernet/TACT1 -> /ethernet.sch/TACT1
- X1 pad 14: Net-(R22-Pad1) -> Net-(R27-Pad1)
- X1 pad 15: Net-(X1-Pad15) -> (no net)
- X1 pad 16: Net-(R23-Pad2) -> Net-(R28-Pad2)
- X1 pad 18: Net-(L1-Pad1) -> Net-(L6-Pad1)
- X1 pad 19: Net-(L1-Pad1) -> Net-(L6-Pad1)
- X1 pad 2: /ethernet/TXRXM_C -> /ethernet.sch/TXRXM_C
- X1 pad 3: /ethernet/TXRXP_C -> /ethernet.sch/TXRXP_C
- X1 pad 4: /ethernet/TXRXP_B -> /ethernet.sch/TXRXP_B
- X1 pad 5: /ethernet/TXRXM_B -> /ethernet.sch/TXRXM_B
- X1 pad 6: /ethernet/TACT2 -> /ethernet.sch/TACT2
- X1 pad 7: /ethernet/TACT4 -> /ethernet.sch/TACT4
- X1 pad 8: /ethernet/TXRXP_D -> /ethernet.sch/TXRXP_D
- X1 pad 9: /ethernet/TXRXM_D -> /ethernet.sch/TXRXM_D
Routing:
- added copper zone on F.Cu, net GND
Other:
- board size 65 x 56.5 mm -> 65 x 56 mm
- copper layers 2 -> 4
- net class Default: trace_width 0.25 -> 0.15; via_dia 0.6 -> 0.4; via_drill 0.4 -> 0.2
- rule pad_to_mask_clearance: 0.2 -> 0.1
- rule trace_min: 0.2 -> 0.15
- rule via_min_drill: 0.3 -> 0.2
- board text added: "If you want to use an SMT 40-pin header, please move the top edge up by 0.5mm and locate the header in the same location as the current TH part."
- board text added: "This is a HAT compatible PCB starting design based on the official Raspberry Pi specs at: https://github.com/raspberrypi/hats/blob/master/designguide.md Currently the camera slot and display cutout are not here. See the schematic for the details on the EEPROM and power setup. This board does have the correct components for powering the Pi via the HAT. If you need the Pi to provide 5V or 3.3V, ple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"
